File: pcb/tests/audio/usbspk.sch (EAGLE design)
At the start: 33 parts, among them J1 SNG-100-HEADER-04-HDR-V, J2 SNG-100-HEADER-02-FL-V, Q1 12MHz, SW1 B3F-1020, SW2 B3F-1020, SW3 B3F-1020, U4 PCM2704C, U5 TPA2005D1DGN

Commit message: Corrected drawings of touch panel PCB
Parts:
- C13: value 100uF -> 100uF 10v
- C14, C15: value (none) -> 18pF
- C18: value 1uF -> 1uF 10v
- C19: value 22nF -> 0.022 uF
- Q1: MFG (none) -> TXC; PART_NO (none) -> 9C-12.000MEEJ-T
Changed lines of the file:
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@@
 <part name="R11" library="Passive" deviceset="RES" device="-0603" value="1.5k"/>
 <part name="C12" library="Passive" deviceset="CAP" device="-0603" value="1uF"/>
-<part name="C13" library="Passive" deviceset="CAP-E" device="-S1210" value="100uF"/>
-<part name="Q1" library="Crystal" deviceset="XTAL" device="HC49S" value="12MHz"/>
-<part name="C14" library="Passive" deviceset="CAP" device="-0603"/>
+<part name="C13" library="Passive" deviceset="CAP-E" device="-S1210" value="100uF 10v"/>
+<part name="Q1" library="Crystal" deviceset="XTAL" device="HC49S" value="12MHz">
+<attribute name="MFG" value="TXC"/>
+<attribute name="PART_NO" value="9C-12.000MEEJ-T"/>
+</part>
+<part name="C14" library="Passive" deviceset="CAP" device="-0603" value="18pF"/>
 <part name="GND18" library="Power" deviceset="GND" device=""/>
 <part name="R12" library="Passive" deviceset="RES" device="-0603" value="1M"/>
-<part name="C15" library="Passive" deviceset="CAP" device="-0603">
+<part name="C15" library="Passive" deviceset="CAP" device="-0603" value="18pF">
 <attribute name="DESCRIPTION" value="{DESCRIPTION} - SMT 0603 - {value}"/>
 <attribute name="PACKAGE" value="SMT 0603"/>
@@
 <part name="C17" library="Passive" deviceset="CAP" device="-0603" value="1uF"/>
 <part name="GND19" library="Power" deviceset="GND" device=""/>
-<part name="C18" library="Passive" deviceset="CAP-E" device="-S0805" value="1uF"/>
+<part name="C18" library="Passive" deviceset="CAP-E" device="-S0805" value="1uF 10v"/>
 <part name="R17" library="Passive" deviceset="RES" device="-0603" value="330"/>
-<part name="C19" library="Passive" deviceset="CAP" device="-0603" value="22nF"/>
+<part name="C19" library="Passive" deviceset="CAP" device="-0603" value="0.022 uF"/>
 <part name="R16" library="Passive" deviceset="RES" device="-0603" value="16"/>
 <part name="GND20" library="Power" deviceset="GND" device=""/>
@@
 <instance part="C12" gate="A" x="134.62" y="139.7"/>
 <instance part="C13" gate="G$1" x="203.2" y="132.08" rot="R90"/>
-<instance part="Q1" gate="G$1" x="195.58" y="195.58"/>
+<instance part="Q1" gate="G$1" x="195.58" y="195.58">
+<attribute name="MFG" x="195.58" y="195.58" size="1.27" layer="96" display="off"/>
+<attribute name="PART_NO" x="195.58" y="195.58" size="1.27" layer="96" display="off"/>
+</instance>
 <instance part="C14" gate="A" x="208.28" y="187.96" rot="R90"/>
 <instance part="GND18" gate="GND" x="213.36" y="180.34"/>

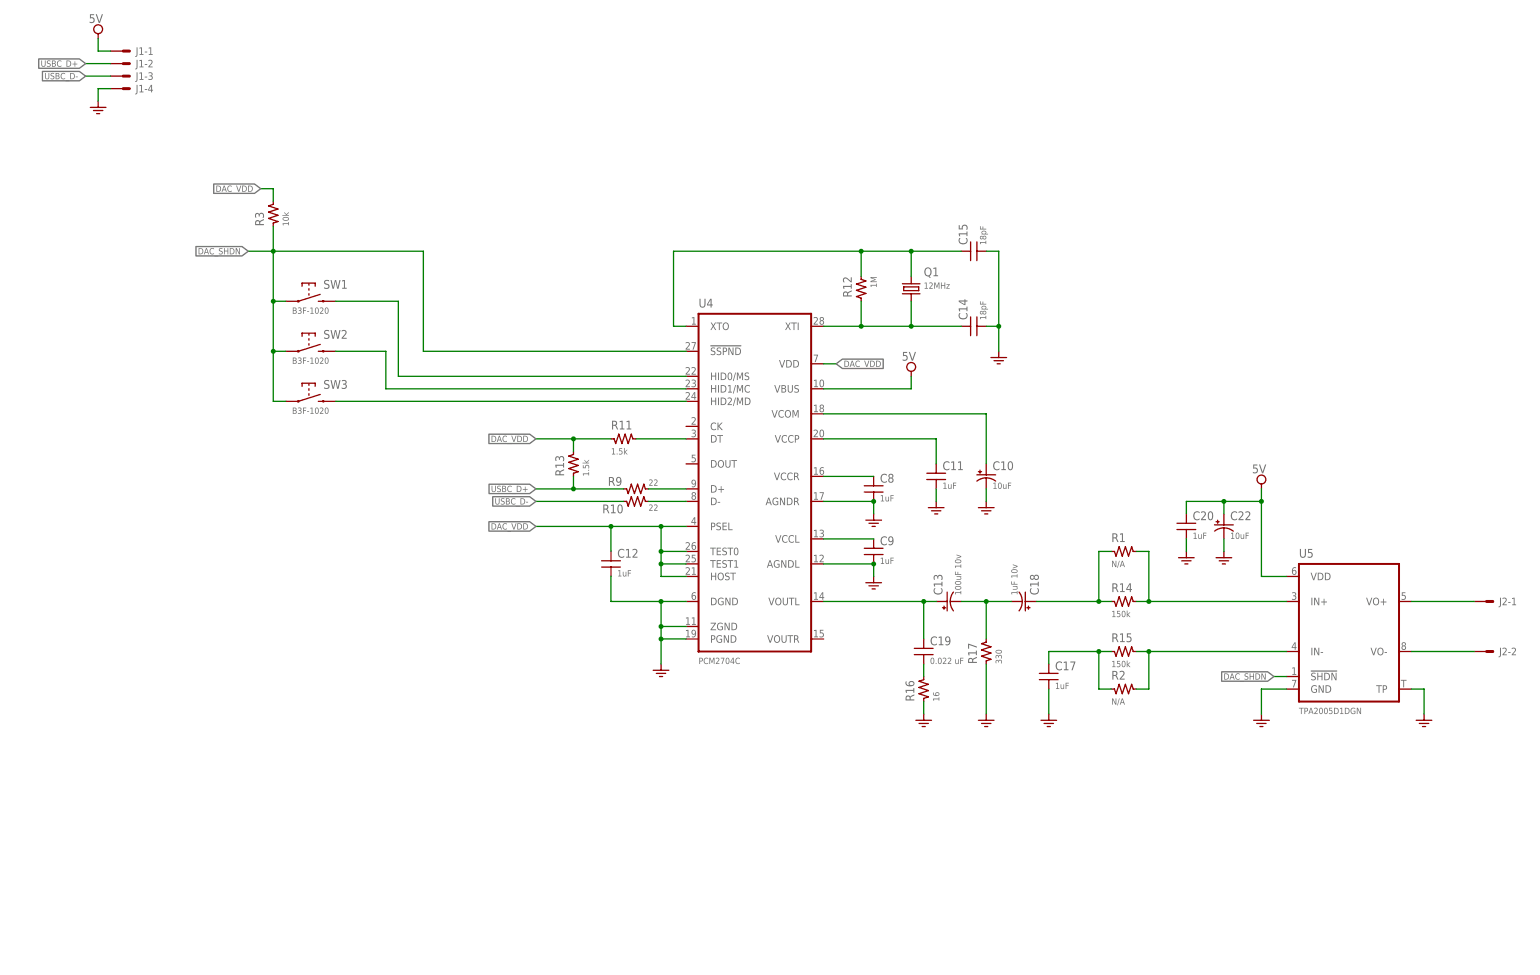
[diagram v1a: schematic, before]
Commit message: Changed page format on schematics to US letter (8.5" x 11")
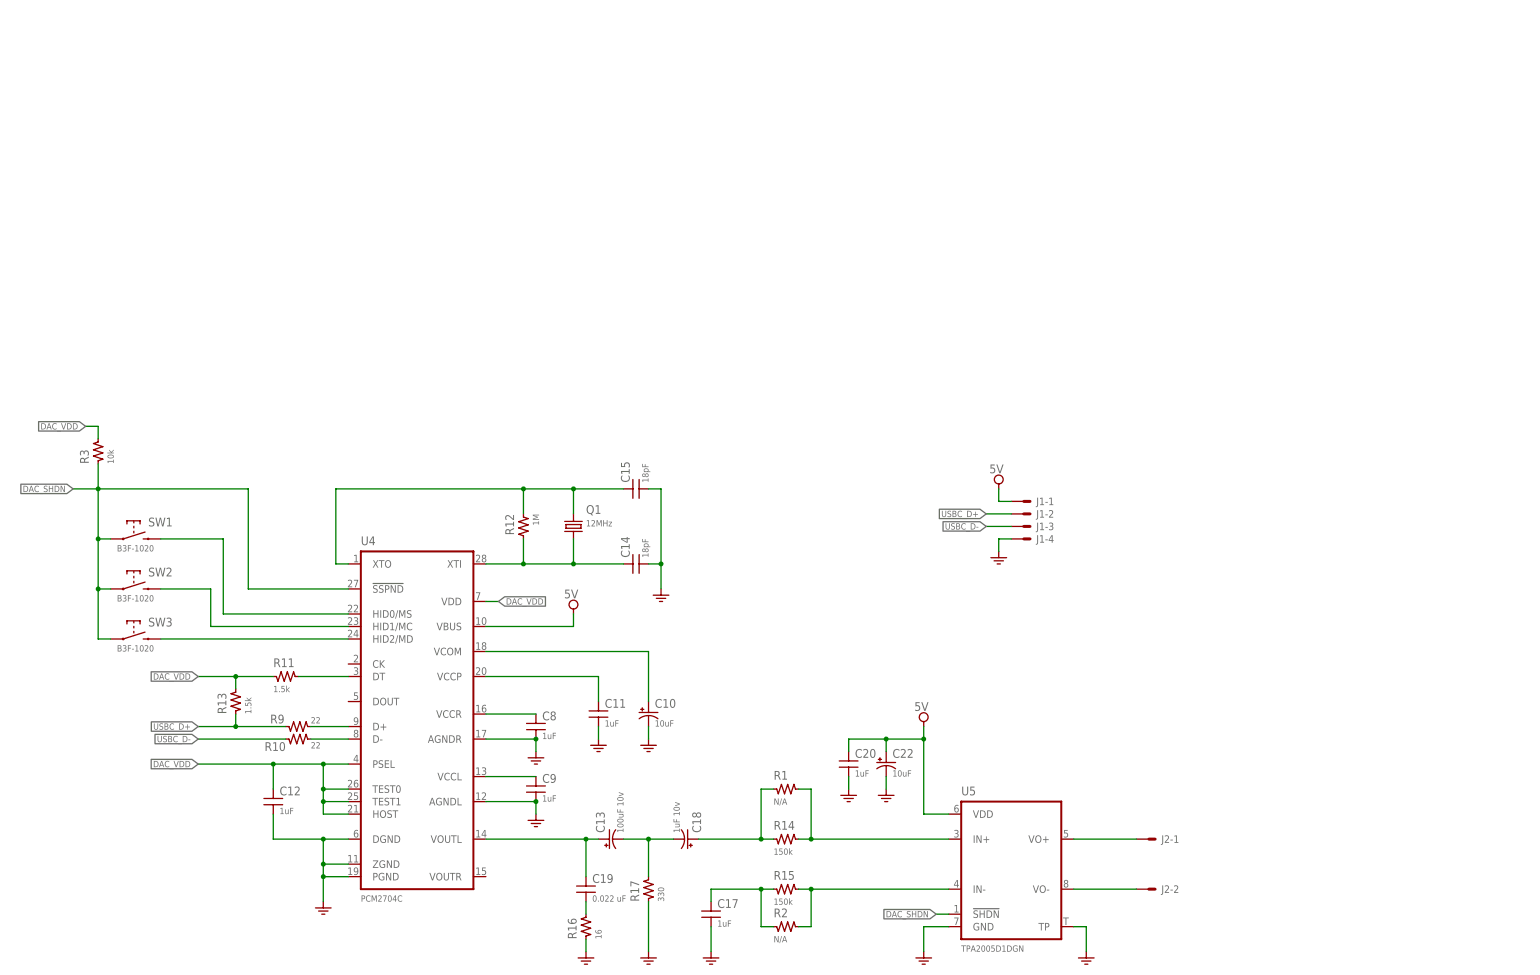
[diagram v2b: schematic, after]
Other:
- moved on the sheet: C10, C11, C12, C13, C14, C15, C17, C18, C19, C20, C22, C8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
